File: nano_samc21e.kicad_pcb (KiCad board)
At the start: 4 copper layers, 18.5 x 38.2 mm, 31 parts, among them J1 SWD, J2 Castellated_headers, SW1 RST, U1 ATSAMC21E18A-M, U2 AP2112K-3.3, U3 LMZM23600V5, Y1 32.768kHz

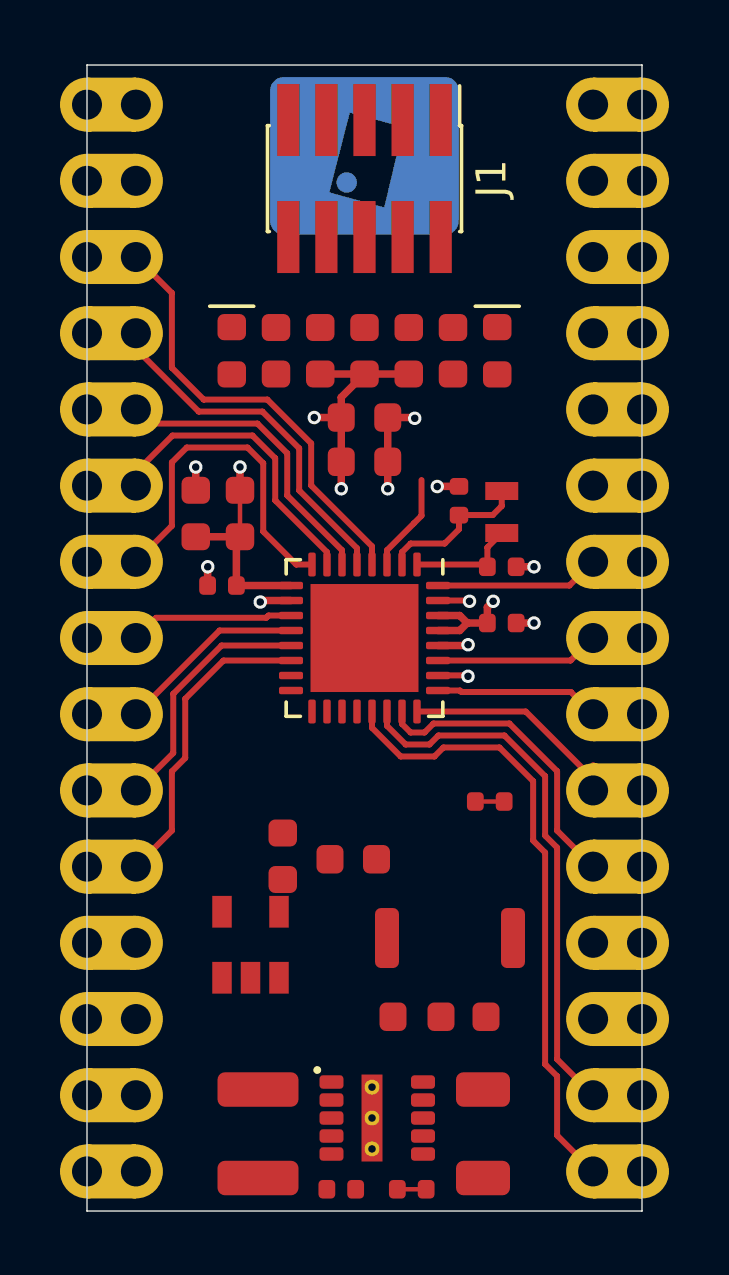
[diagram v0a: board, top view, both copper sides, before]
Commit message: Massive rework: - 2 layer PCB - design restraints set according to JLCPCB capabilites - no castellated holes, smaller board dimensions - Arduino style numbering on top silkscreen - Changed footprints to match JLCPCB basic parts TODO: layout and routing
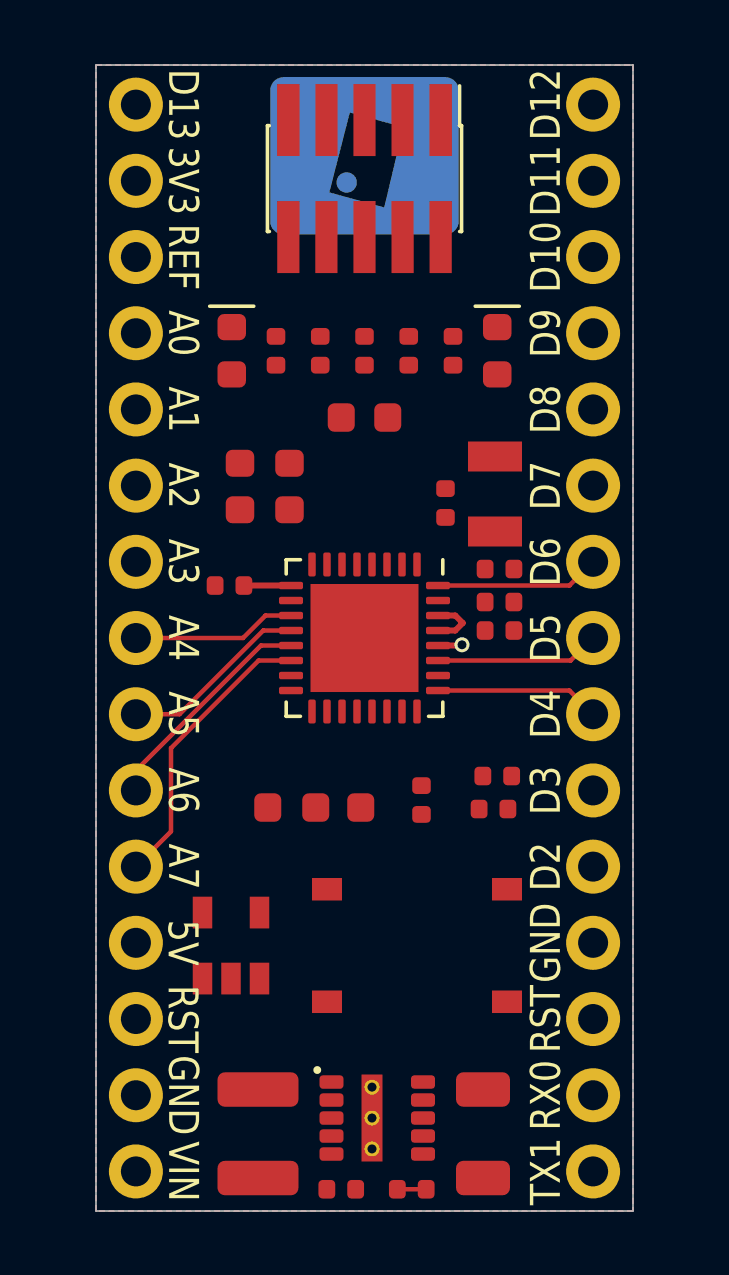
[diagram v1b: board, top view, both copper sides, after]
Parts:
- C1, C10, C11, C3, R1, R3, R4, R5: footprint global:0603_minimalist -> global:0402_minimalist
- C7, C8: value 2p -> 15p
- FB1: value NC -> 470R; footprint global:0603_NC_minimalist -> global:0603_minimalist
- J2: footprint global:Arduino_Nano_castellated -> global:Arduino_Nano
- R2: value NC -> 330; footprint global:0402_NC_minimalist -> global:0402_minimalist
- SW1: footprint global:SW_Push_Alps_SKRK -> Button_Switch_SMD:SW_SPST_SKQG_WithStem
- Y1: value 32.768kHz -> 32.768kHz 12.5p; footprint Crystal:Crystal_SMD_2012-2Pin_2.0x1.2mm -> Crystal:Crystal_SMD_3215-2Pin_3.2x1.5mm
- moved JP1 8.13 mm to (23.4, 39.9)
- moved C3 6.49 mm to (28.8, 33.0)
- moved C11 5.54 mm to (28.7, 38.9)
- moved C10 4.99 mm to (26.1, 39.6)
- moved FB1 1.88 mm to (21.8, 29.2)
- moved C5 1.73 mm to (20.1, 29.2)
- moved SW1 1.13 mm to (26.0, 44.5)
- moved U2 0.65 mm to (19.8, 44.5)
- moved Y1 0.64 mm to (28.6, 29.4)
- moved C8 0.46 mm to (26.9, 29.8)
- moved R2 0.28 mm to (28.6, 40.0), turned to 180 degrees
- moved C4 0.26 mm to (28.8, 34.0)
- moved C6 0.25 mm to (19.8, 32.5)
- moved C7 0.11 mm to (28.8, 31.9)
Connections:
- net D0_TX renamed D1_TX
- J2 pad 2: D1_RX -> D0_RX
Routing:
- net D1_TX: track 20.7 -> 0.00 mm
- net D1_RX: track 18.0 -> 0.00 mm
- net AREF: track 14.8 -> 0.00 mm
- net A0: track 12.0 -> 0.00 mm
- net A3: track 11.6 -> 0.00 mm
- net VCC: track 12.4 -> 1.86 mm, vias 4 -> 0
- net A2: track 10.2 -> 0.00 mm
- net D2: track 10.2 -> 0.00 mm
- net A1: track 10.1 -> 0.00 mm
- net D3: track 8.03 -> 0.00 mm
- net GND: track 8.66 -> 0.81 mm, vias 9 -> 1
- net XOUT32: track 5.15 -> 0.00 mm
- net XIN32: track 3.70 -> 0.00 mm
- net VAA: track 4.97 -> 1.57 mm
- net D9: track 3.29 -> 0.00 mm
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- added copper zone on B.Cu, net GND
- added copper zone on F.Cu, net GND
- removed copper zone on In1.Cu, net GND
- removed copper zone on In2.Cu, net VCC
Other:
- board size 18.5 x 38.2 mm -> 17.9 x 38.2 mm
- copper layers 4 -> 2

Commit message: v1.0 finished - layout and routing finished - added front and back graphics, JLCPCB tooling holes
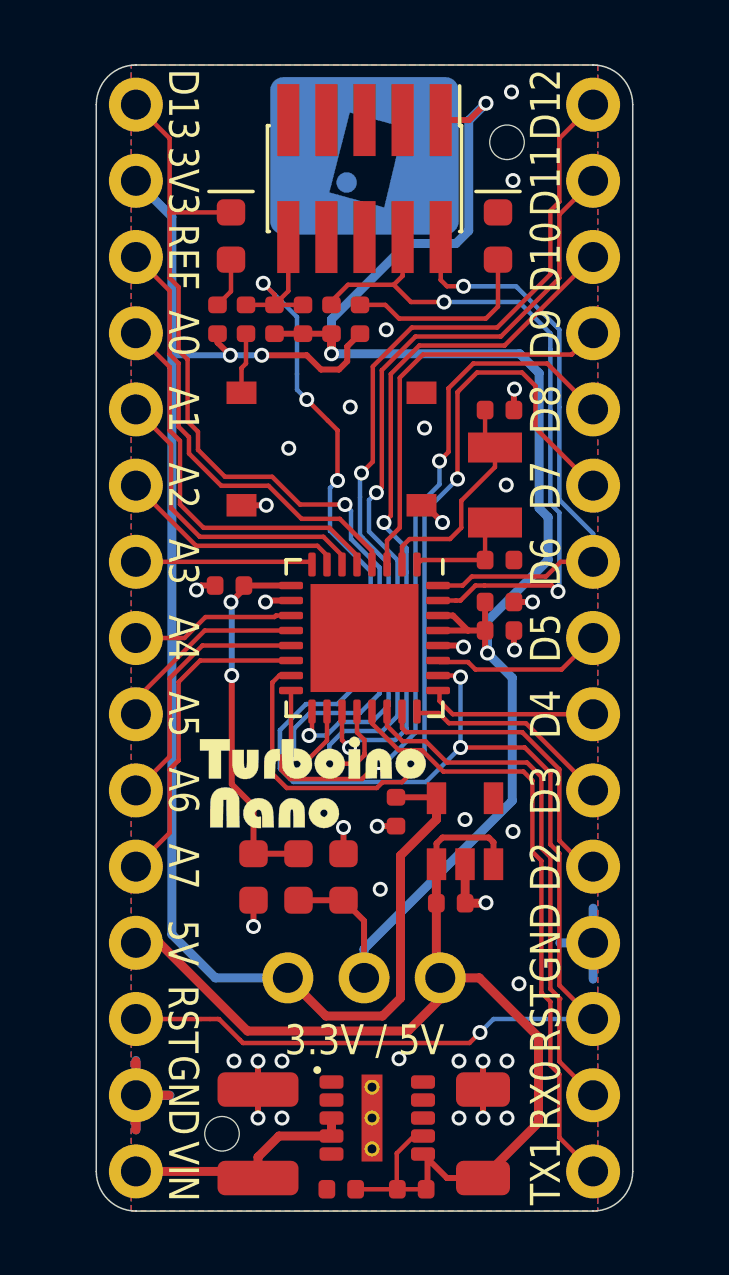
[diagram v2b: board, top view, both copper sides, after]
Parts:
- added FID2: Tooling, global:JLCPCB_tooling_hole, F.Cu at (19.5, 50.8)
- added FID3: Tooling, global:JLCPCB_tooling_hole, F.Cu at (29.0, 17.7)
- added FID4: Logo2, global:turboino_logo, F.Cu at (24.2, 34.3)
- added FID5: Logo3, global:turboino_back, B.Cu at (24.2, 34.1)
- D2: value PWR -> USER
- JP1: footprint global:0603_3pos_jumper -> Connector_PinHeader_2.54mm:PinHeader_1x03_P2.54mm_Vertical
- moved R2 18.3 mm to (20.3, 23.6), turned to 90 degrees
- moved SW1 16.8 mm to (23.1, 27.9)
- moved C2 15.3 mm to (23.6, 42.2), turned to 90 degrees
- moved C5 13.0 mm to (20.6, 42.2), turned to -90 degrees
- moved FB1 13.0 mm to (22.1, 42.2), turned to -90 degrees
- moved U2 8.68 mm to (27.6, 40.7)
- moved JP1 6.63 mm to (26.8, 45.6), turned to -90 degrees
- moved D1 3.83 mm to (28.7, 20.9)
- moved D2 3.83 mm to (19.8, 20.9)
- moved C8 3.58 mm to (28.8, 26.6), turned to 0 degrees
- moved C11 3.58 mm to (25.3, 40.0), turned to -90 degrees
- moved C10 3.57 mm to (27.1, 43.1), turned to 0 degrees
- moved R4 3.27 mm to (24.1, 23.6), turned to 90 degrees
- moved R3 2.78 mm to (23.1, 23.6)
- moved R1 2.30 mm to (22.2, 23.6)
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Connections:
- U1 pad 22: D1_RX -> D0_RX
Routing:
- net RST: track 0.00 -> 62.8 mm, vias 0 -> 6
- net VCC: track 1.86 -> 55.3 mm, vias 0 -> 3
- net +3V3: track 0.00 -> 51.3 mm, vias 0 -> 2
- net D13_SCK: track 0.00 -> 33.7 mm, vias 0 -> 2
- net +5V: track 0.00 -> 32.9 mm
- net D7: track 0.00 -> 29.3 mm, vias 0 -> 2
- net D12_CIPO: track 0.00 -> 29.2 mm, vias 0 -> 2
- net D11_COPI: track 0.00 -> 29.1 mm, vias 0 -> 2
- net D8: track 0.00 -> 25.7 mm, vias 0 -> 2
- net D10_SS: track 0.00 -> 24.1 mm, vias 0 -> 2
- net GND: track 0.81 -> 24.8 mm, vias 1 -> 35
- net SWDCLK: track 0.00 -> 23.1 mm, vias 0 -> 2
- net D1_TX: track 0.00 -> 20.4 mm
- net D0_RX: track 0.00 -> 17.7 mm
- net AREF: track 0.00 -> 15.2 mm
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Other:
- outline, holes or cut-outs redrawn
- board text added: "3.3V / 5V"
